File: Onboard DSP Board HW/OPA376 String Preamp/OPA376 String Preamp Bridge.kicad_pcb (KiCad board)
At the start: 2 copper layers, 28.4 x 92.7 mm, 48 parts, among them J1 Input, J10 Input, J14 Input, J5 Input, U1 TLV9001IDCK, U2 TLV9001IDCK, U3 TLV9001IDCK, U4 TLV9001IDCK

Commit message: WIP
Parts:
- C1, C11, C13, C15: footprint Capacitor_SMD:C_0402_1005Metric -> Capacitor_SMD:C_0603_1608Metric
- C2: value C -> 10uF; footprint Capacitor_SMD:C_0402_1005Metric -> Capacitor_SMD:C_0603_1608Metric
- J9: footprint Connector_JST:JST_SH_SM06B-SRSS-TB_1x06-1MP_P1.00mm_Horizontal -> Connector_PinHeader_2.00mm:PinHeader_1x06_P2.00mm_Horizontal
- R1: value R -> 100K
- R2: value R -> 43K
- U1, U2, U3, U4: value TLV9001IDCK -> OPA376
- moved R1 45.0 mm to (101.6, 100.0), turned to 90 degrees
- moved C2 45.0 mm to (100.2, 100.0), turned to -90 degrees
- moved R2 44.0 mm to (102.7, 100.0), turned to -90 degrees
- moved J9 5.30 mm to (94.9, 57.2), turned to -90 degrees
- moved C15 1.08 mm to (96.5, 128.0), turned to 0 degrees
- moved C13 1.07 mm to (96.5, 109.8), turned to 0 degrees
- moved C1 0.99 mm to (96.6, 73.8), turned to 0 degrees
- moved C11 0.98 mm to (96.6, 91.6), turned to 0 degrees
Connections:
- C2 pad 1: /SIngle FET preamp/3.3V -> /SIngle FET preamp/MidRail
- J9 pad 1: /SIngle FET preamp/3.3V -> GND
- J9 pad 2: /SIngle FET preamp/Output -> /SIngle FET preamp3/Output
- J9 pad 3: /SIngle FET preamp1/Output -> /SIngle FET preamp2/Output
- J9 pad 4: /SIngle FET preamp2/Output -> /SIngle FET preamp1/Output
- J9 pad 5: /SIngle FET preamp3/Output -> /SIngle FET preamp/Output
- J9 pad 6: GND -> /SIngle FET preamp/3.3V
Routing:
- net GND: track 16.4 -> 9.89 mm, vias 29 -> 27
- net /SIngle FET preamp/3.3V: track 104.0 -> 97.9 mm
- net /SIngle FET preamp/MidRail: track 81.2 -> 85.6 mm
- net /SIngle FET preamp2/Output: track 58.5 -> 59.8 mm
- net /SIngle FET preamp1/Output: track 40.5 -> 41.4 mm
- net /SIngle FET preamp/Output: track 21.5 -> 20.6 mm
- net Net-(C15-Pad2): track 1.11 -> 1.70 mm
- net Net-(C13-Pad2): track 1.11 -> 1.68 mm
- net Net-(C11-Pad2): track 1.11 -> 1.62 mm
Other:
- board text added: "V+"

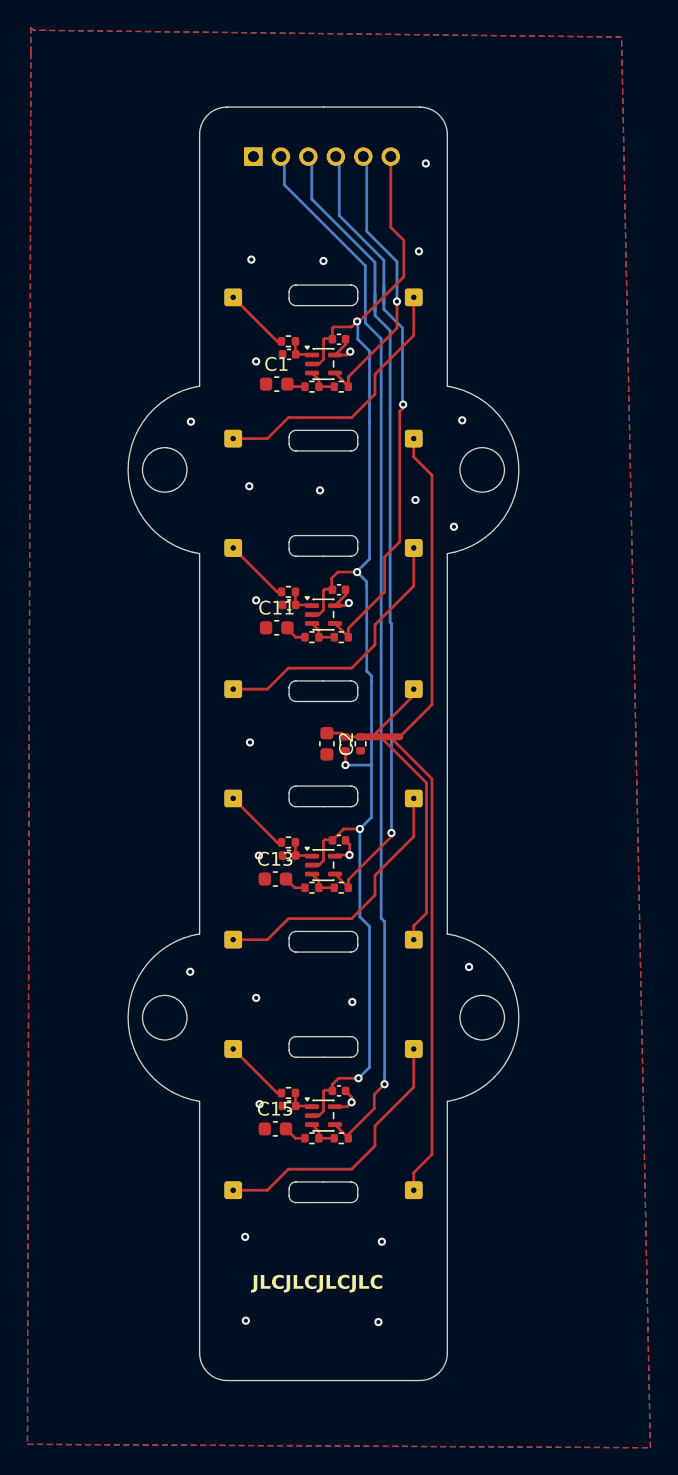
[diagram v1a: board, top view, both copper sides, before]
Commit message: Fix Opamp supplies, simulate, add safety resistor to V+
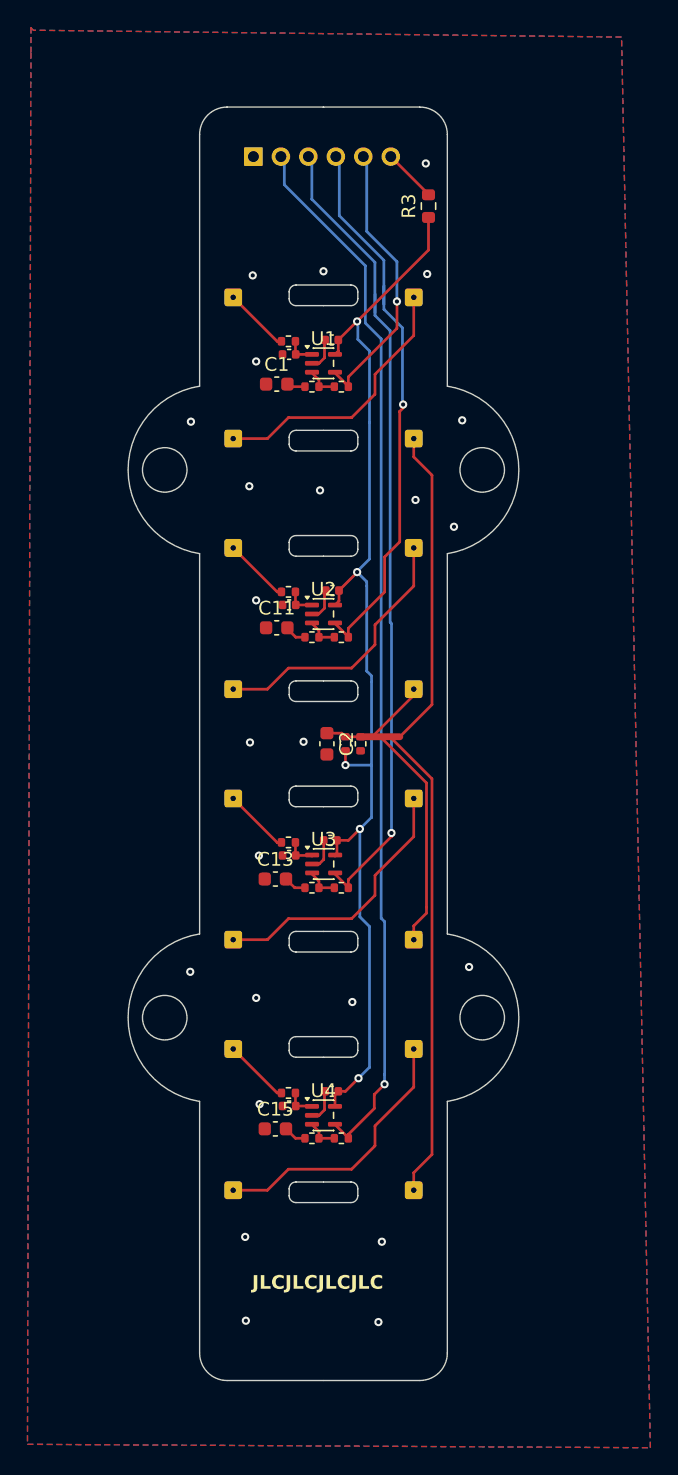
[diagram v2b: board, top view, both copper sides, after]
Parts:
- added R3: 47, Resistor_SMD:R_0603_1608Metric, F.Cu at (107.6, 60.9)
- U1, U2, U3, U4: value OPA376 -> OPA376xxDCK
- moved C19 0.63 mm to (100.5, 107.0), turned to 180 degrees
- moved C17 0.53 mm to (100.6, 70.6), turned to 180 degrees
- moved C20 0.53 mm to (100.6, 125.3), turned to 180 degrees
- moved C18 0.48 mm to (100.7, 88.8), turned to 180 degrees
- moved U3 0.08 mm to (100.0, 108.8)
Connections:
- net Net-(J1-Pin_1) renamed /Input
- net Net-(J10-Pin_1) renamed /SIngle FET preamp2/Input
- net Net-(J14-Pin_1) renamed /SIngle FET preamp3/Input
- net Net-(J5-Pin_1) renamed /SIngle FET preamp1/Input
- J9 pad 6: /SIngle FET preamp/3.3V -> Net-(J9-Pin_6)
- U1 pad 2: /SIngle FET preamp/3.3V -> GND
- U1 pad 5: GND -> /SIngle FET preamp/3.3V
- U2 pad 2: /SIngle FET preamp/3.3V -> GND
- U2 pad 5: GND -> /SIngle FET preamp/3.3V
- U3 pad 2: /SIngle FET preamp/3.3V -> GND
- U3 pad 5: GND -> /SIngle FET preamp/3.3V
- U4 pad 2: /SIngle FET preamp/3.3V -> GND
- U4 pad 5: GND -> /SIngle FET preamp/3.3V
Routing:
- net /SIngle FET preamp/3.3V: track 97.9 -> 82.6 mm
- net Net-(J9-Pin_6): track 0.00 -> 4.07 mm
- net GND: track 9.89 -> 9.63 mm, vias 27 -> 22
- net (no net): vias 0 -> 2

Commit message: WIP
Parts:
- U1, U2, U3, U4: value OPA376xxDCK -> OPA376AIDCKT
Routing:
- net GND: vias 22 -> 24
- net (no net): vias 2 -> 0

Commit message: WIP
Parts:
- removed C2: 10uF, Capacitor_SMD:C_0603_1608Metric
- removed J9: ~, Connector_PinHeader_2.00mm:PinHeader_1x06_P2.00mm_Horizontal
- removed R1: 100K, Resistor_SMD:R_0402_1005Metric
- added C21: 220pF, Capacitor_SMD:C_0402_1005Metric, F.Cu at (101.4, 129.8)
- added C3: 100nF, Capacitor_SMD:C_0603_1608Metric, F.Cu at (107.7, 64.6)
- added J18: ~, Connector_PinHeader_2.00mm:PinHeader_1x07_P2.00mm_Horizontal, B.Cu at (93.8, 57.7)
- added R25: 27K, Resistor_SMD:R_0402_1005Metric, F.Cu at (97.4, 72.7)
- added R26: 27K, Resistor_SMD:R_0402_1005Metric, F.Cu at (97.4, 91.0)
- added R27: 27K, Resistor_SMD:R_0402_1005Metric, F.Cu at (97.4, 109.2)
- added R28: 27K, Resistor_SMD:R_0402_1005Metric, F.Cu at (97.4, 127.4)
- added U5: OPA376AIDCKR, Package_TO_SOT_SMD:SOT-353_SC-70-5, F.Cu at (101.3, 100.0)
- C1: value 22uF -> 100pF; footprint Capacitor_SMD:C_0603_1608Metric -> Capacitor_SMD:C_0402_1005Metric
- C11, C13, C15: value 22uF -> 220pF; footprint Capacitor_SMD:C_0603_1608Metric -> Capacitor_SMD:C_0402_1005Metric
- R2: value 43K -> 1K
- U1, U2, U3, U4: value OPA376AIDCKT -> OPA376AIDCKR
- moved C1 25.9 mm to (99.2, 99.6), turned to -90 degrees
- moved C11 17.1 mm to (100.8, 75.0), turned to 180 degrees
- moved C13 17.1 mm to (100.7, 93.3), turned to 180 degrees
- moved C15 17.1 mm to (101.0, 111.6), turned to 180 degrees
- moved R2 4.67 mm to (98.0, 99.6), turned to 90 degrees
- moved R3 0.35 mm to (107.7, 61.2), turned to -90 degrees
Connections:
- net /Input renamed /SIngle FET preamp/in
- net /SIngle FET preamp1/Input renamed /SIngle FET preamp1/in
- net /SIngle FET preamp2/Input renamed /SIngle FET preamp2/in
- net /SIngle FET preamp3/Input renamed /SIngle FET preamp3/in
- C1 pad 1: GND -> Net-(U5-+)
- C1 pad 2: Net-(C1-Pad2) -> GND
- C11 pad 1: GND -> /SIngle FET preamp/Output
- C11 pad 2: Net-(C11-Pad2) -> Net-(U1--)
- C13 pad 1: GND -> /SIngle FET preamp1/Output
- C13 pad 2: Net-(C13-Pad2) -> Net-(U2--)
- C15 pad 1: GND -> /SIngle FET preamp2/Output
- C15 pad 2: Net-(C15-Pad2) -> Net-(U3--)
- R14 pad 1: Net-(C1-Pad2) -> /SIngle FET preamp/MidRail
- R17 pad 1: Net-(C11-Pad2) -> /SIngle FET preamp/MidRail
- R2 pad 1: /SIngle FET preamp/MidRail -> /Bias
- R2 pad 2: GND -> Net-(U5-+)
- R20 pad 1: Net-(C13-Pad2) -> /SIngle FET preamp/MidRail
- R23 pad 1: Net-(C15-Pad2) -> /SIngle FET preamp/MidRail
- R3 pad 1: /SIngle FET preamp/3.3V -> /3V3
- R3 pad 2: Net-(J9-Pin_6) -> /SIngle FET preamp/3.3V
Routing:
- net /SIngle FET preamp/MidRail: track 85.6 -> 135.1 mm, vias 0 -> 8
- net /Bias: track 0.00 -> 49.2 mm, vias 0 -> 1
- net /3V3: track 0.00 -> 10.9 mm
- net Net-(J9-Pin_6): track 4.07 -> 0.00 mm
- net GND: track 9.63 -> 12.4 mm, vias 24 -> 32
- net Net-(U5-+): track 0.00 -> 2.55 mm
- net /SIngle FET preamp1/Output: track 41.4 -> 39.5 mm
- net Net-(C15-Pad2): track 1.70 -> 0.00 mm
- net Net-(C13-Pad2): track 1.68 -> 0.00 mm
- net Net-(C11-Pad2): track 1.62 -> 0.00 mm
- net Net-(C1-Pad2): track 1.40 -> 0.00 mm
- net Net-(U2--): track 2.33 -> 3.64 mm
- net Net-(U3--): track 2.33 -> 3.54 mm
- net Net-(U4--): track 2.33 -> 3.52 mm
- net Net-(U1--): track 2.33 -> 3.47 mm
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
